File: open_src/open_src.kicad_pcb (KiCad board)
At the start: 2 copper layers, 54 x 83 mm, 44 parts, among them J1 AVR-JTAG-10, Q1 BTA12-800BWRG, Q2 2STR1215, Q3 2STR2160, SW1 SW_DPST_x2, U1 MGM240PB32VNA3, U2 ACS712xLCTR-05B, U3 MOC3021S, U4 AMS1117-3.3

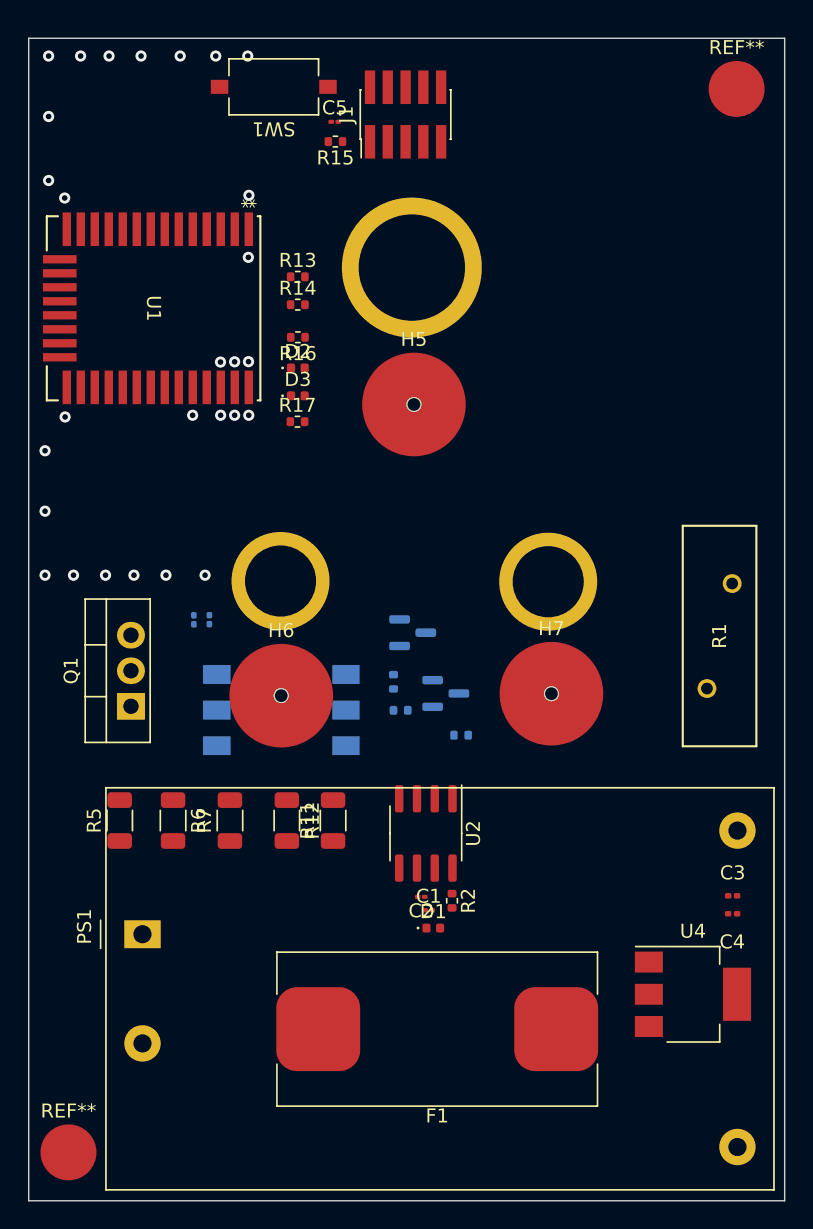
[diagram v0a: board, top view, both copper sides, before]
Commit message: Added trace
Still not yet cross checked
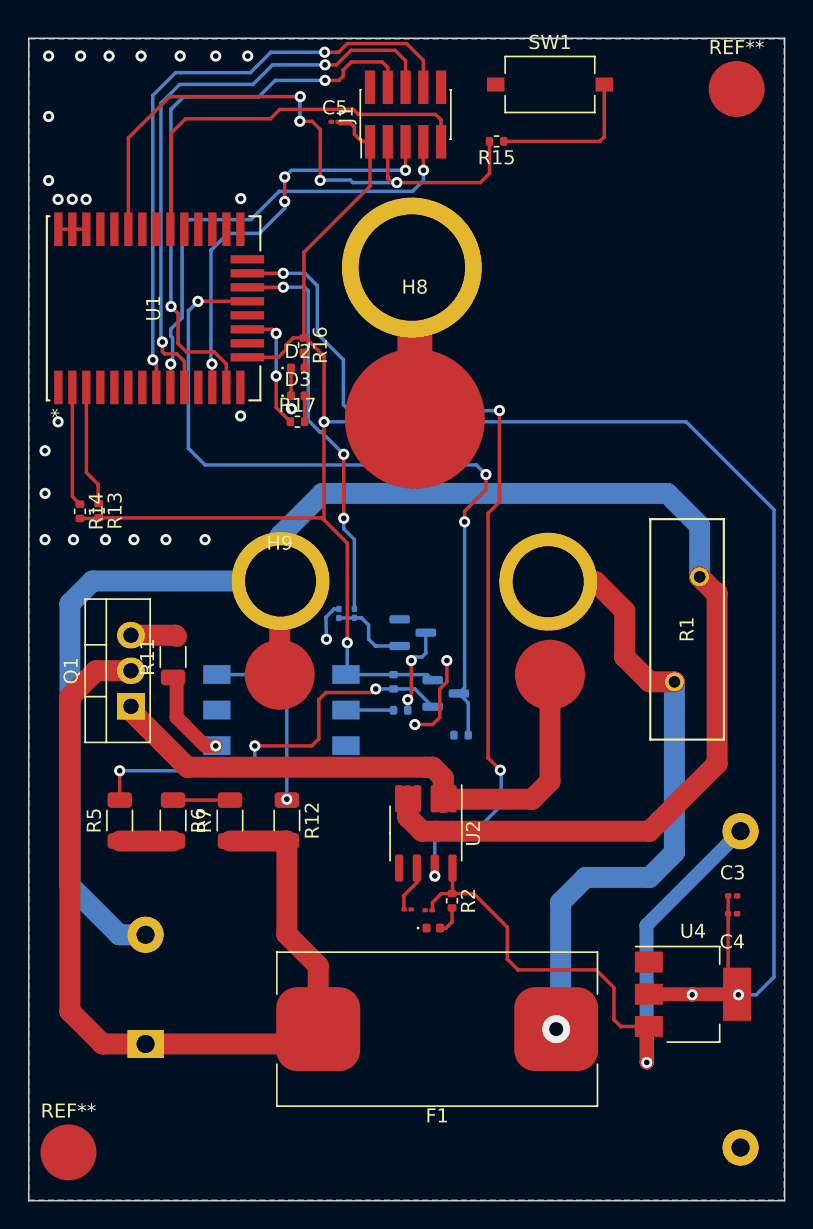
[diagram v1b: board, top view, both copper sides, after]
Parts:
- removed H5: Earth, Mounting_Wuerth:Mounting_Wuerth_WA-SMSE-ExternalM3_H8mm_9771080360
- removed H6: Neutral, Mounting_Wuerth:Mounting_Wuerth_WA-SMSE-ExternalM3_H5mm_9771050360
- removed H7: Phase_OUT, Mounting_Wuerth:Mounting_Wuerth_WA-SMSE-ExternalM3_H5mm_9771050360
- added H4: Phase_OUT, MountingHole:MountingHole_8.4mm_M8_Pad, F.Cu at (173.7, 98.8)
- added H8: Earth, MountingHole:MountingHole_8.4mm_M8_Pad, F.Cu at (164.1, 80.5)
- added H9: Neutral, MountingHole:MountingHole_8.4mm_M8_Pad, F.Cu at (154.4, 98.8)
- PS1: moved to B.Cu
- moved R13 21.9 mm to (141.5, 87.1), turned to -90 degrees
- moved R14 21.4 mm to (140.2, 87.1), turned to -90 degrees
- moved SW1 19.7 mm to (173.7, 56.6), turned to 0 degrees
- moved R11 16.3 mm to (146.8, 97.5)
- moved R15 11.5 mm to (169.9, 60.7)
- moved R8 10.4 mm to (158.7, 94.4)
- moved R9 10.4 mm to (159.8, 94.4)
- moved PS1 7.84 mm to (144.8, 125.2)
- moved R1 2.37 mm to (182.6, 99.3)
- moved C2 1.32 mm to (163.6, 115.6)
- moved R16 0.71 mm to (156.2, 75.3), turned to -90 degrees
- turned U1 to 90 degrees
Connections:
- U1 pad 1: (no net) -> GND
- U1 pad 14: (no net) -> GND
- U1 pad 15: (no net) -> +3.3v
- U1 pad 23: (no net) -> GND
- U1 pad 32: (no net) -> GND
- U1 pad 34: (no net) -> GND
- U1 pad 35: (no net) -> GND
- U1 pad 36: (no net) -> GND
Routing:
- net +3.3v: track 0.00 -> 158.2 mm, vias 0 -> 4
- net Neutral: track 0.00 -> 128.4 mm
- net Phase_SCR: track 0.00 -> 65.2 mm
- net Current_monitor: track 0.00 -> 63.5 mm, vias 0 -> 4
- net ZCR_OUT: track 0.00 -> 56.0 mm, vias 0 -> 3
- net +5v: track 0.00 -> 46.7 mm, vias 0 -> 1
- net RESET: track 0.00 -> 45.3 mm, vias 0 -> 4
- net Phase_IN: track 0.00 -> 44.9 mm, vias 0 -> 1
- net SWCLK: track 0.00 -> 44.2 mm, vias 0 -> 2
- net SW0: track 0.00 -> 42.7 mm, vias 0 -> 2
- net Phase_OUT: track 0.00 -> 42.4 mm
- net RX: track 0.00 -> 41.4 mm, vias 0 -> 2
- net SWDIO: track 0.00 -> 33.3 mm, vias 0 -> 2
- net Net-(Q3-B): track 0.00 -> 29.6 mm, vias 0 -> 3
- net TX: track 0.00 -> 29.4 mm, vias 0 -> 4
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- added copper zone on B.Cu, net GND
- added copper zone on F.Cu, net GND
